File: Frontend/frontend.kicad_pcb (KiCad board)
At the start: 4 copper layers, 100 x 100.2 mm, 353 parts, among them J1 VOCM, J10 SWD, J11 APWR, J2 BNC, J3 UMC, J4 UMC, J5 VOCM, J6 BNC, J7 UMC, J8 UMC, J9 PCIEx4 EDGE, K1 HE3600, K2 EE2-5NU, K3 HE3600, K4 HE3600, K5 EE2-5NU, K6 HE3600, Q1 ULN2003AD, U1 MCP9700T-E/TT, U10 ADA4817-1ACPZ, U11 MAX4567EEE, U12 MAX4567EEE, U13 MAX4567EEE, U14 AD8003ACPZ, U15 LMH6552SD, U16 MC33078DGK, U17 MAX5725AAUP, U18 STM32F030C8T, U19 MC33078DGK, U2 ADA4817-1ACPZ, U20 MC33078DGK, U21 MC33078DGK, U22 MC33078DGK, U23 LM317S, U24 MCP9700T-E/TT, U25 L78M05CDT, U26 TLV70233DSE, U27 MCP9700T-E/TT, U28 MC79M05CDT, U3 MAX4567EEE, U4 MAX4567EEE, U5 MAX4567EEE, U6 AD8003ACPZ, U7 LMH6552SD, U8 MC33078DGK, U9 MCP9700T-E/TT

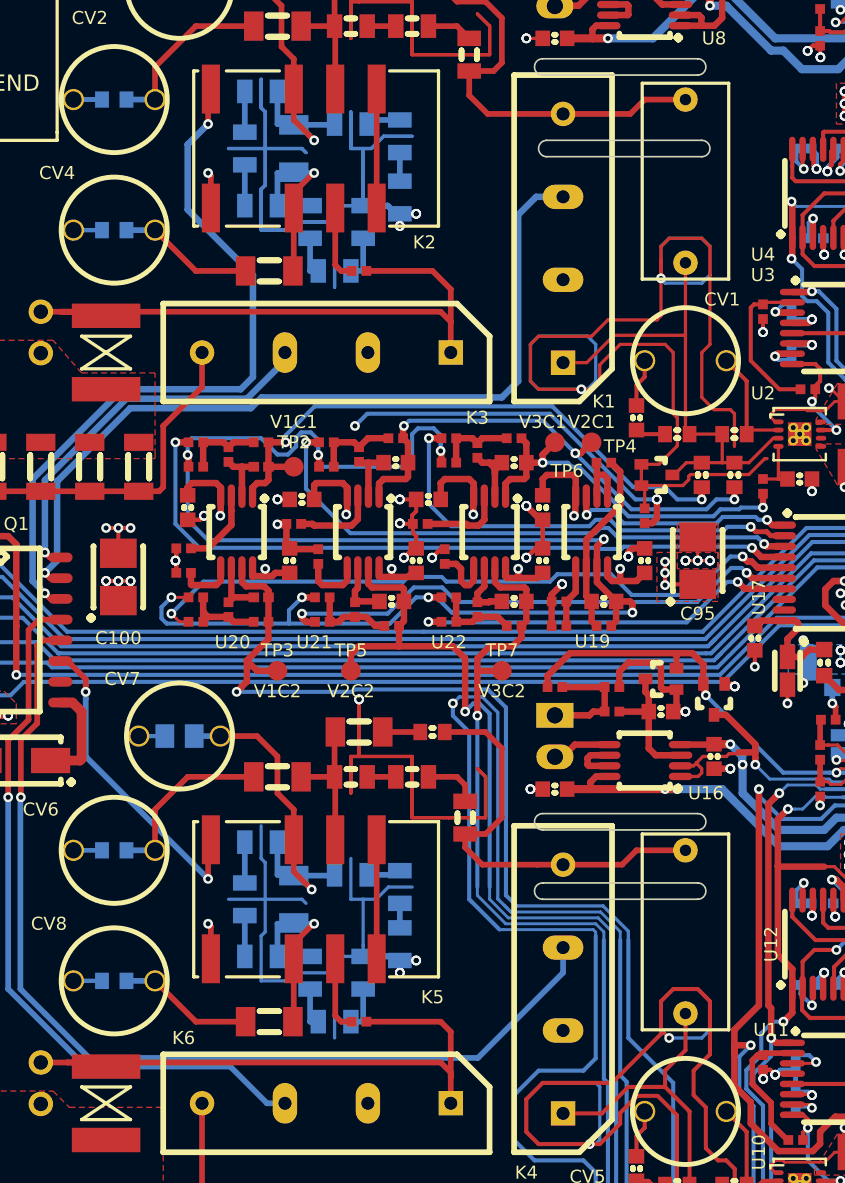
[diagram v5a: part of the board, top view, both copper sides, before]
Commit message: Add bypass capacitor around AC coupling capacitors
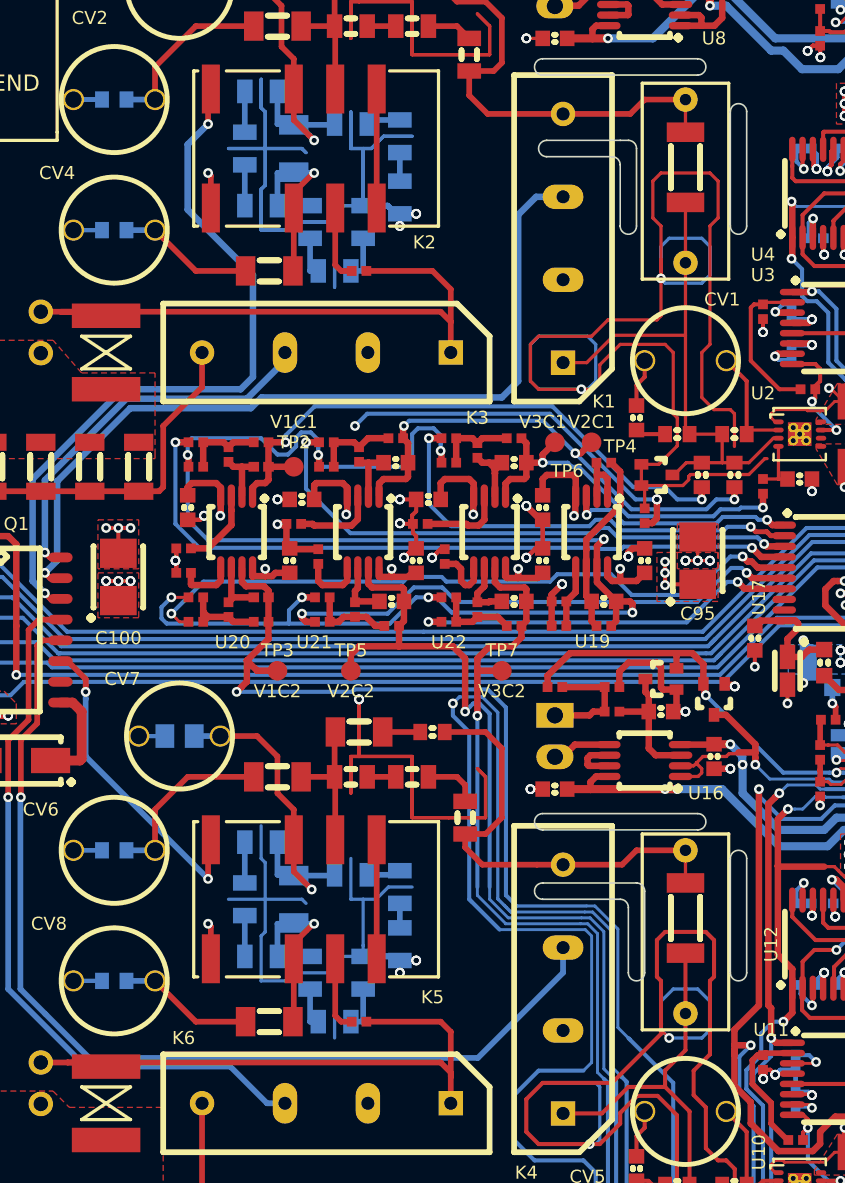
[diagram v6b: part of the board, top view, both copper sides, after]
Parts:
- added C117: 1n 2kV, IPC7351-Nominal:CAPC4520X168, F.Cu at (114.5, 83.2)
- added C18: 1n 2kV, IPC7351-Nominal:CAPC4520X168, F.Cu at (114.5, 37.1)
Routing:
- net /Channel1/GUARD: track 88.2 -> 97.6 mm
- net /Channel2/GUARD: track 88.8 -> 97.0 mm
- net Net-(C18-Pad1): track 30.0 -> 33.7 mm
- net Net-(C117-Pad1): track 29.4 -> 33.1 mm
- net Net-(C18-Pad2): track 25.4 -> 27.4 mm
- net Net-(C117-Pad2): track 26.1 -> 28.1 mm
- net GND: track 1254.7 -> 1254.0 mm
- added copper zone on F.Cu, net -8
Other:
- outline, holes or cut-outs redrawn

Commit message: Reannotate after adding parts
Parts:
- removed the C101 at (105.8, 58.0)
- added C103: 100n, IPC7351-Nominal:CAPC1608X55, F.Cu at (105.8, 58.0)
- renumbered C9 to C10, C98 to C100, C99 to C101, C100 to C102, C102 to C104, C103 to C105, C104 to C106, C105 to C107, C106 to C108, C107 to C109, C10 to C11, C108 to C110, C109 to C111, C110 to C112, C111 to C113, C112 to C114, C113 to C115, C114 to C116, C115 to C117, C116 to C118, C11 to C12, C12 to C13, C13 to C14, C14 to C15, C15 to C16, C16 to C17, C17 to C18, C19 to C20, C20 to C21, C21 to C22, C22 to C23, C23 to C24, C24 to C25, C25 to C26, C26 to C27, C27 to C28, C28 to C29, C29 to C30, C30 to C31, C31 to C32, C32 to C33, C33 to C34, C34 to C35, C35 to C36, C36 to C37, C37 to C38, C38 to C39, C18 to C4, C39 to C40, C40 to C41, C41 to C42, C117 to C43, C42 to C44, C43 to C45, C44 to C46, C45 to C47, C46 to C48, C47 to C49, C4 to C5, C48 to C50, C49 to C51, C50 to C52, C51 to C53, C52 to C54, C53 to C55, C54 to C56, C55 to C57, C56 to C58, C57 to C59, C5 to C6, C58 to C60, C59 to C61, C60 to C62, C61 to C63, C62 to C64, C63 to C65, C64 to C66, C65 to C67, C66 to C68, C67 to C69, C6 to C7, C68 to C70, C69 to C71, C70 to C72, C71 to C73, C72 to C74, C73 to C75, C74 to C76, C75 to C77, C76 to C78, C77 to C79, C7 to C8, C78 to C80, C79 to C81, C80 to C82, C81 to C83, C82 to C84, C83 to C85, C84 to C86, C85 to C87, C86 to C88, C87 to C89, C8 to C9, C88 to C90, C89 to C91, C90 to C92, C91 to C93, C92 to C94, C93 to C95, C94 to C96, C95 to C97, C96 to C98, C97 to C99
